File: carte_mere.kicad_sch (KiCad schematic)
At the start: 77 parts, among them J10 Conn_01x02_Pin, J11 Conn_01x02_Pin, J12 Conn_01x02_Pin, J13 Conn_01x03_Pin, J14 Conn_01x02, J20 Conn_01x04, J23 Conn_01x02, J24 Conn_01x02, J25 Conn_01x03_Pin, J26 Conn_01x03_Pin, J27 Conn_01x03_Pin, J28 Conn_01x03_Pin, J29 Conn_01x03_Pin, J30 Conn_01x03_Pin, J41 Conn_01x06_Pin, J42 Conn_01x06_Pin, J43 Conn_01x02_Pin, Q35 2N7002

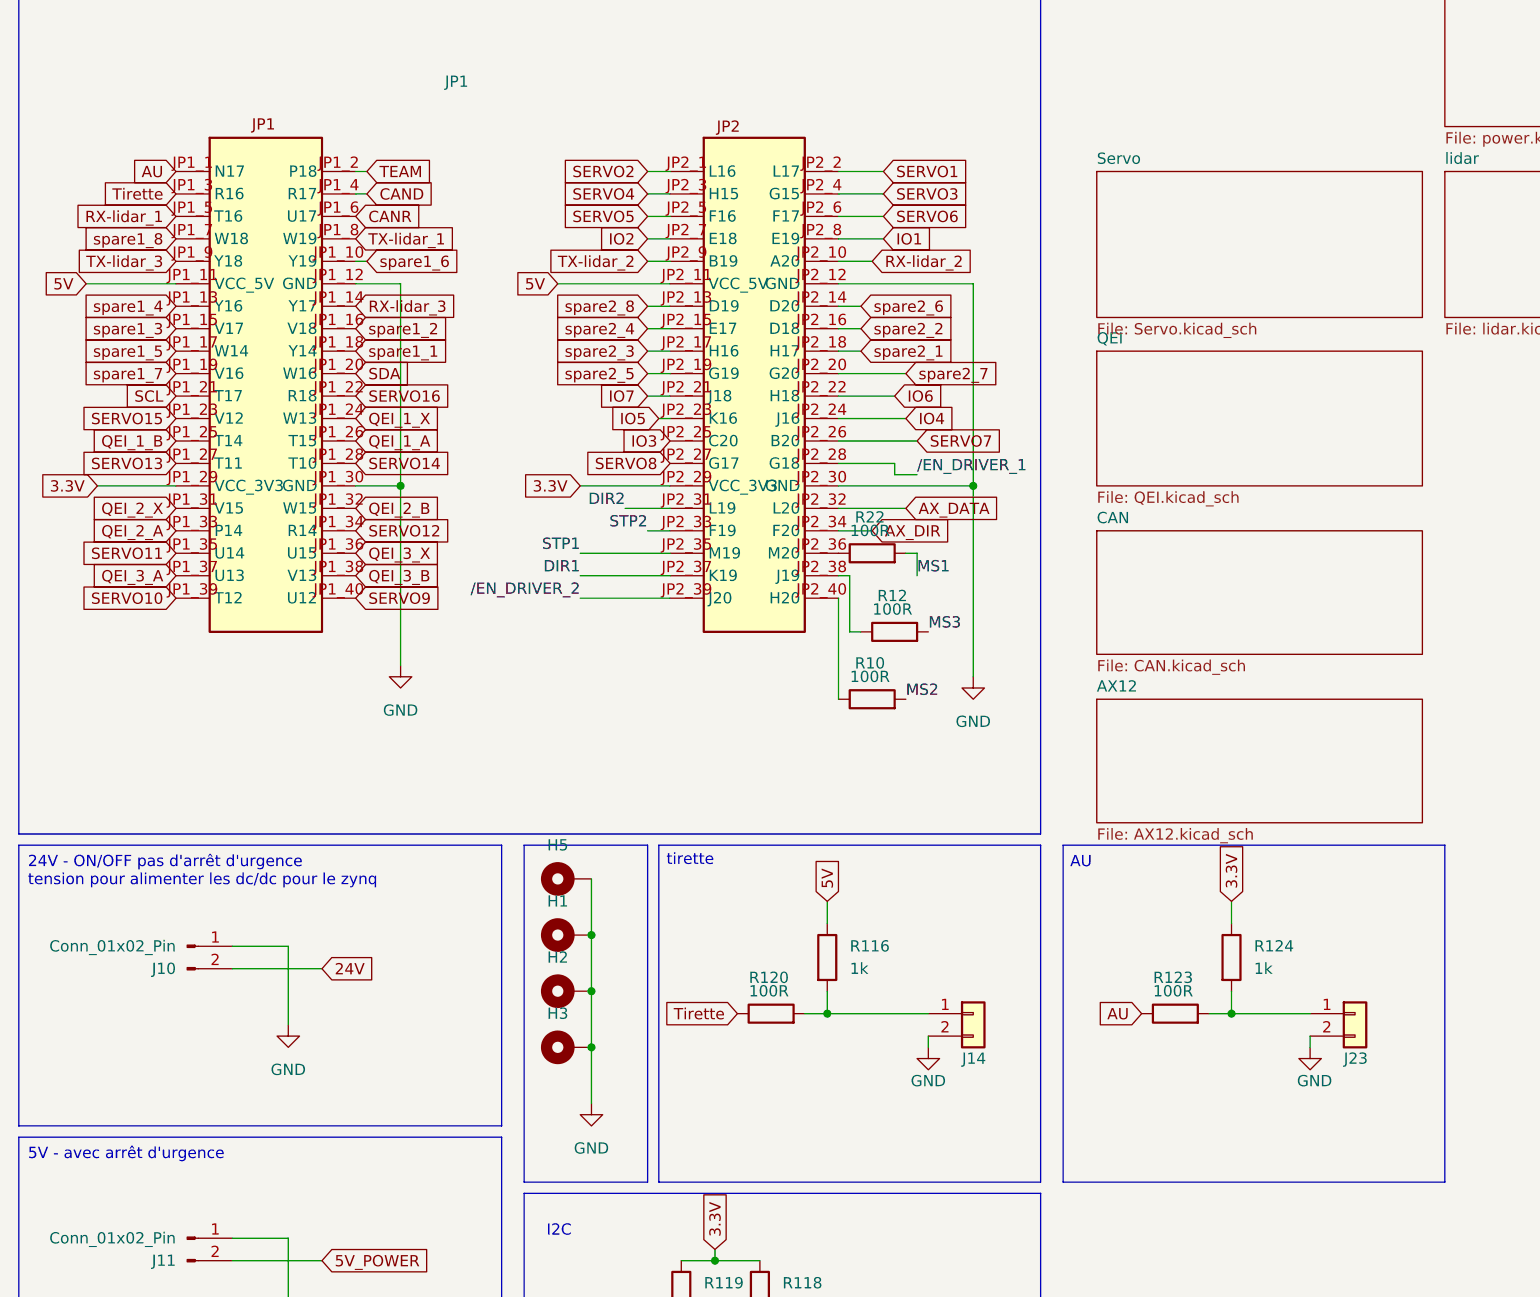
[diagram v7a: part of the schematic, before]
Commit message: update zynq footprint
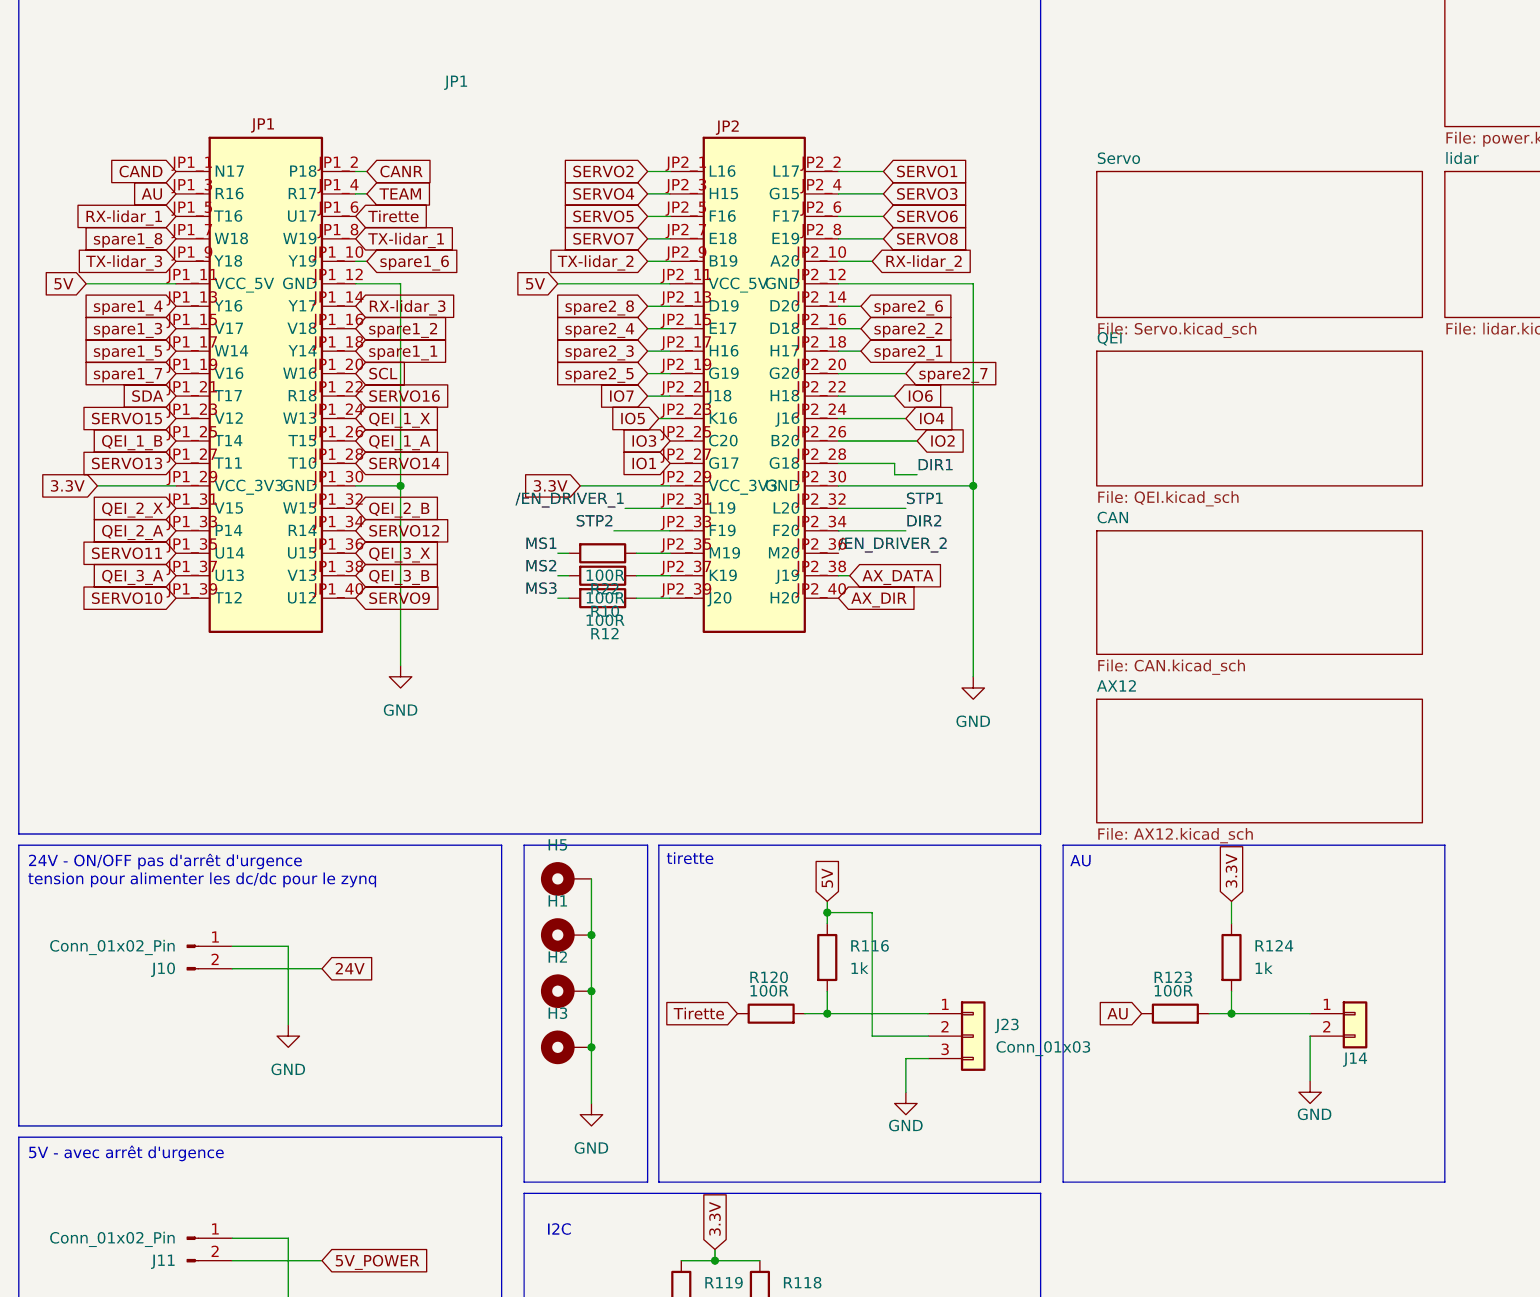
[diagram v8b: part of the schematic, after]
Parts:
- removed J23: Conn_01x02, Connector_Molex:Molex_KK-254_AE-6410-02A_1x02_P2.54mm_Vertical, symbol Connector_Generic:Conn_01x02
- added J23: Conn_01x03, 7Robot_Conn:JST_XH_B3B-XH-A_1x03_P2.50mm_Vertical, symbol Connector_Generic:Conn_01x03
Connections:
- net 5V: now also J23.2 (Pin_2)
- net AU: now also JP1.JP1_3 (R16); no longer JP1.JP1_1 (N17)
- net AX_DATA: now also JP1.JP2_38 (J19); no longer JP1.JP2_32 (L20)
- net AX_DIR: now also JP1.JP2_40 (H20); no longer JP1.JP2_34 (F20)
- net CAND: now also JP1.JP1_1 (N17); no longer JP1.JP1_4 (R17)
- net CANR: now also JP1.JP1_2 (P18); no longer JP1.JP1_6 (U17)
- net DIR1: now also JP1.JP2_28 (G18); no longer JP1.JP2_37 (K19)
- net DIR2: now also JP1.JP2_34 (F20); no longer JP1.JP2_31 (L19)
- net GND: now also J23.3 (Pin_3)
- net IO1: now also JP1.JP2_27 (G17); no longer JP1.JP2_8 (E19)
- net IO2: now also JP1.JP2_26 (B20); no longer JP1.JP2_7 (E18)
- net SCL: now also JP1.JP1_20 (W16); no longer JP1.JP1_21 (T17)
- net SDA: now also JP1.JP1_21 (T17); no longer JP1.JP1_20 (W16)
- net SERVO7: now also JP1.JP2_7 (E18); no longer JP1.JP2_26 (B20)
- net SERVO8: now also JP1.JP2_8 (E19); no longer JP1.JP2_27 (G17)
- net STP1: now also JP1.JP2_32 (L20); no longer JP1.JP2_35 (M19)
- net TEAM: now also JP1.JP1_4 (R17); no longer JP1.JP1_2 (P18)
- net Tirette: now also JP1.JP1_6 (U17); no longer JP1.JP1_3 (R16)
- net /EN_DRIVER_1: now also JP1.JP2_31 (L19); no longer JP1.JP2_28 (G18)
- net /EN_DRIVER_2: now also JP1.JP2_36 (M20); no longer JP1.JP2_39 (J20)
- net at R123.2, R124.2: now also J14.1 (Pin_1)
- net at R116.2, R120.2: now also J23.1 (Pin_1); no longer J14.1 (Pin_1)
- net at R22.1: now also JP1.JP2_35 (M19); no longer JP1.JP2_36 (M20)
- net at R12.1: now also JP1.JP2_39 (J20); no longer JP1.JP2_38 (J19)
- net at R10.1: now also JP1.JP2_37 (K19); no longer JP1.JP2_40 (H20)
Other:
- moved on the sheet: R10, R22
